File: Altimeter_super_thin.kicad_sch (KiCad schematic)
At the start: 58 parts, among them IC1 XTSD02GLGEAG, J1 Conn_01x04_Male, J2 Conn_01x02_Male, Q1 PMV20ENR, U1 150044M155220, U2 ESP32-S3, U4 DPS310, Y1 40MHz±10ppm

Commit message: initial stage of reitteration
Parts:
- removed C12: 4.2pF, Capacitor_SMD:C_0402_1005Metric, symbol Device:C_Small
- removed R8: 47.5, Resistor_SMD:R_0402_1005Metric, symbol Device:R_Small
- IC1: footprint iclr:SOTFL50P160X60-8N -> iclr:SON127P800X600X95-8N
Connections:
- net +3.3V is gone; now on net +3V3: U1.1 (V)
- no-connect marks 21 -> 22
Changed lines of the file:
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@@
 (kicad_sch (version 20230121) (generator eeschema)
   (paper "A4")
-  (junction (at 39.37 21.59) (diameter 0) (color 0 0 0 0)
-  )
   (junction (at 59.69 142.24) (diameter 0) (color 0 0 0 0)
   )
@@
   )
   (junction (at 69.85 135.89) (diameter 0) (color 0 0 0 0)
+  )
+  (junction (at 40.64 21.59) (diameter 0) (color 0 0 0 0)
   )
   (junction (at 271.78 52.07) (diameter 0) (color 0 0 0 0)
@@
   (no_connect (at 135.89 72.39))
   (no_connect (at 135.89 113.03))
+  (no_connect (at 69.85 62.23))
   (no_connect (at 135.89 82.55))
   (no_connect (at 135.89 85.09))
@@
     (stroke (width 0) (type default))
   )
-  (wire (pts (xy 68.58 62.23) (xy 69.85 62.23))
-    (stroke (width 0) (type default))
-  )
   (wire (pts (xy 27.94 21.59) (xy 30.48 21.59))
     (stroke (width 0) (type default))
@@
     (stroke (width 0) (type default))
   )
-  (wire (pts (xy 50.8 62.23) (xy 54.61 62.23))
-    (stroke (width 0) (type default))
-  )
   (wire (pts (xy 210.82 93.98) (xy 210.82 59.69))
     (stroke (width 0) (type default))
@@
     (stroke (width 0) (type default))
   )
-  (wire (pts (xy 59.69 62.23) (xy 63.5 62.23))
-    (stroke (width 0) (type default))
-  )
   (wire (pts (xy 34.29 167.64) (xy 34.29 165.1))
     (stroke (width 0) (type default))
@@
     (stroke (width 0) (type default))
   )
-  (wire (pts (xy 35.56 21.59) (xy 39.37 21.59))
+  (wire (pts (xy 35.56 21.59) (xy 40.64 21.59))
     (stroke (width 0) (type default))
   )
@@
     (stroke (width 0) (type default))
   )
+  (wire (pts (xy 40.64 21.59) (xy 44.45 21.59))
+    (stroke (width 0) (type default))
+  )
   (wire (pts (xy 201.93 80.01) (xy 233.68 80.01))
     (stroke (width 0) (type default))
@@
   )
   (wire (pts (xy 167.64 127) (xy 167.64 132.08))
-    (stroke (width 0) (type default))
-  )
-  (wire (pts (xy 39.37 21.59) (xy 44.45 21.59))
     (stroke (width 0) (type default))
   )
@@
     )
   )
-  (symbol (lib_id "power:+3.3V") (at 39.37 21.59 0) (unit 1)
-    (in_bom yes) (on_board yes) (dnp no)
-    (property "Reference" "#PWR08" (at 39.37 25.4 0)
-      (effects (font (size 1.27 1.27)) hide)
-    )
-    (property "Value" "+3.3V" (at 39.751 17.1958 0)
-      (effects (font (size 1.27 1.27)))
-    )
-    (property "Footprint" "" (at 39.37 21.59 0)
-      (effects (font (size 1.27 1.27)) hide)
-    )
-    (property "Datasheet" "" (at 39.37 21.59 0)
-      (effects (font (size 1.27 1.27)) hide)
-    )
-    (pin "1")
-    (instances
-      (project "Altimeter"
-        (path "/7db990e4-92e1-4f99-b4d2-435bbec1ba83"
-          (reference "#PWR08") (unit 1)
-        )
-      )
-    )
-  )
   (symbol (lib_id "Device:LED_Small") (at 54.61 21.59 180) (unit 1)
     (in_bom yes) (on_board yes) (dnp no)
@@
     )
   )
+  (symbol (lib_id "power:+3V3") (at 19.05 69.85 0) (unit 1)
+    (in_bom yes) (on_board yes) (dnp no)
+    (property "Reference" "#PWR09" (at 19.05 73.66 0)
+      (effects (font (size 1.27 1.27)) hide)
+    )
+    (property "Value" "+3V3" (at 15.24 68.58 0)
+      (effects (font (size 1.27 1.27)))
+    )
+    (property "Footprint" "" (at 19.05 69.85 0)
+      (effects (font (size 1.27 1.27)) hide)
+    )
+    (property "Datasheet" "" (at 19.05 69.85 0)
+      (effects (font (size 1.27 1.27)) hide)
+    )
+    (pin "1")
+    (instances
+      (project "Altimeter"
+        (path "/7db990e4-92e1-4f99-b4d2-435bbec1ba83"
+          (reference "#PWR09") (unit 1)
+        )
+      )
+    )
+  )
   (symbol (lib_id "Connector:TestPoint") (at 69.85 118.11 90) (unit 1)
     (in_bom yes) (on_board yes) (dnp no)
@@
       (effects (font (size 1.27 1.27)))
     )
-    (property "Footprint" "iclr:SOTFL50P160X60-8N" (at 39.37 96.52 0)
+    (property "Footprint" "iclr:SON127P800X600X95-8N" (at 39.37 96.52 0)
       (effects (font (size 1.27 1.27)) (justify left) hide)
     )
@@
     )
   )
-  (symbol (lib_name "+3.3V_1") (lib_id "power:+3.3V") (at 19.05 69.85 0) (unit 1)
-    (in_bom yes) (on_board yes) (dnp no)
-    (property "Reference" "#PWR09" (at 19.05 73.66 0)
-      (effects (font (size 1.27 1.27)) hide)
-    )
-    (property "Value" "+3.3V" (at 15.24 67.31 0)
-      (effects (font (size 1.27 1.27)))
-    )
-    (property "Footprint" "" (at 19.05 69.85 0)
-      (effects (font (size 1.27 1.27)) hide)
-    )
-    (property "Datasheet" "" (at 19.05 69.85 0)
-      (effects (font (size 1.27 1.27)) hide)
-    )
-    (pin "1")
-    (instances
-      (project "Altimeter"
-        (path "/7db990e4-92e1-4f99-b4d2-435bbec1ba83"
-          (reference "#PWR09") (unit 1)
-        )
-      )
-    )
-  )
   (symbol (lib_id "Device:R") (at 43.18 71.12 90) (unit 1)
     (in_bom yes) (on_board yes) (dnp no)
@@
     )
   )
-  (symbol (lib_id "Device:C_Small") (at 66.04 62.23 90) (unit 1)
-    (in_bom yes) (on_board yes) (dnp no)
-    (property "Reference" "C12" (at 67.31 57.15 90)
-      (effects (font (size 1.27 1.27)) (justify left))
-    )
-    (property "Value" "4.2pF" (at 66.2934 59.2481 90)
-      (effects (font (size 1.27 1.27)) (justify left))
-    )
-    (property "Footprint" "Capacitor_SMD:C_0402_1005Metric" (at 66.04 62.23 0)
-      (effects (font (size 1.27 1.27)) hide)
-    )
-    (property "Datasheet" "~" (at 66.04 62.23 0)
-      (effects (font (size 1.27 1.27)) hide)
-    )
-    (pin "1")
-    (pin "2")
-    (instances
-      (project "Altimeter"
-        (path "/7db990e4-92e1-4f99-b4d2-435bbec1ba83"
-          (reference "C12") (unit 1)
-        )
-      )
-    )
-  )
   (symbol (lib_id "Connector:TestPoint") (at 143.51 80.01 180) (unit 1)
     (in_bom yes) (on_board yes) (dnp no)
@@
         (path "/7db990e4-92e1-4f99-b4d2-435bbec1ba83"
           (reference "TP10") (unit 1)
+        )
+      )
+    )
+  )
+  (symbol (lib_id "power:+3V3") (at 40.64 21.59 0) (unit 1)
+    (in_bom yes) (on_board yes) (dnp no) (fields_autoplaced)
+    (property "Reference" "#PWR012" (at 40.64 25.4 0)
+      (effects (font (size 1.27 1.27)) hide)
+    )
+    (property "Value" "+3V3" (at 40.64 16.51 0)
+      (effects (font (size 1.27 1.27)))
+    )
+    (property "Footprint" "" (at 40.64 21.59 0)
+      (effects (font (size 1.27 1.27)) hide)
+    )
+    (property "Datasheet" "" (at 40.64 21.59 0)
+      (effects (font (size 1.27 1.27)) hide)
+    )
+    (pin "1")
+    (instances
+      (project "Altimeter"
+        (path "/7db990e4-92e1-4f99-b4d2-435bbec1ba83"
+          (reference "#PWR012") (unit 1)
         )
       )
@@
         )
       )
-    )
-  )
-  (symbol (lib_id "power:GND") (at 50.8 62.23 0) (unit 1)
-    (in_bom yes) (on_board yes) (dnp no)
-    (property "Reference" "#PWR012" (at 50.8 68.58 0)
-      (effects (font (size 1.27 1.27)) hide)
-    )
-    (property "Value" "GND" (at 48.26 66.04 0)
-      (effects (font (size 1.27 1.27)) (justify left))
-    )
-    (property "Footprint" "" (at 50.8 62.23 0)
-      (effects (font (size 1.27 1.27)) hide)
-    )
-    (property "Datasheet" "" (at 50.8 62.23 0)
-      (effects (font (size 1.27 1.27)) hide)
-    )
-    (pin "1")
-    (instances
-      (project "Altimeter"
-        (path "/7db990e4-92e1-4f99-b4d2-435bbec1ba83"
-          (reference "#PWR012") (unit 1)
-        )
-      )
-    )
-  )
-  (symbol (lib_id "Device:R_Small") (at 57.15 62.23 90) (unit 1)
-    (in_bom yes) (on_board yes) (dnp no)
-    (property "Reference" "R8" (at 57.15 57.15 90)
-      (effects (font (size 1.27 1.27)))
-    )
-    (property "Value" "47.5" (at 57.15 59.69 90)
-      (effects (font (size 1.27 1.27)))
-    )
-    (property "Footprint" "Resistor_SMD:R_0402_1005Metric" (at 57.15 62.23 0)
-      (effects (font (size 1.27 1.27)) hide)
-    )
-    (property "Datasheet" "~" (at 57.15 62.23 0)
-      (effects (font (size 1.27 1.27)) hide)
-    )
-    (pin "1")
-    (pin "2")
-    (instances
-      (project "Altimeter"
-        (path "/7db990e4-92e1-4f99-b4d2-435bbec1ba83"
-          (reference "R8") (unit 1)
-        )
-      )

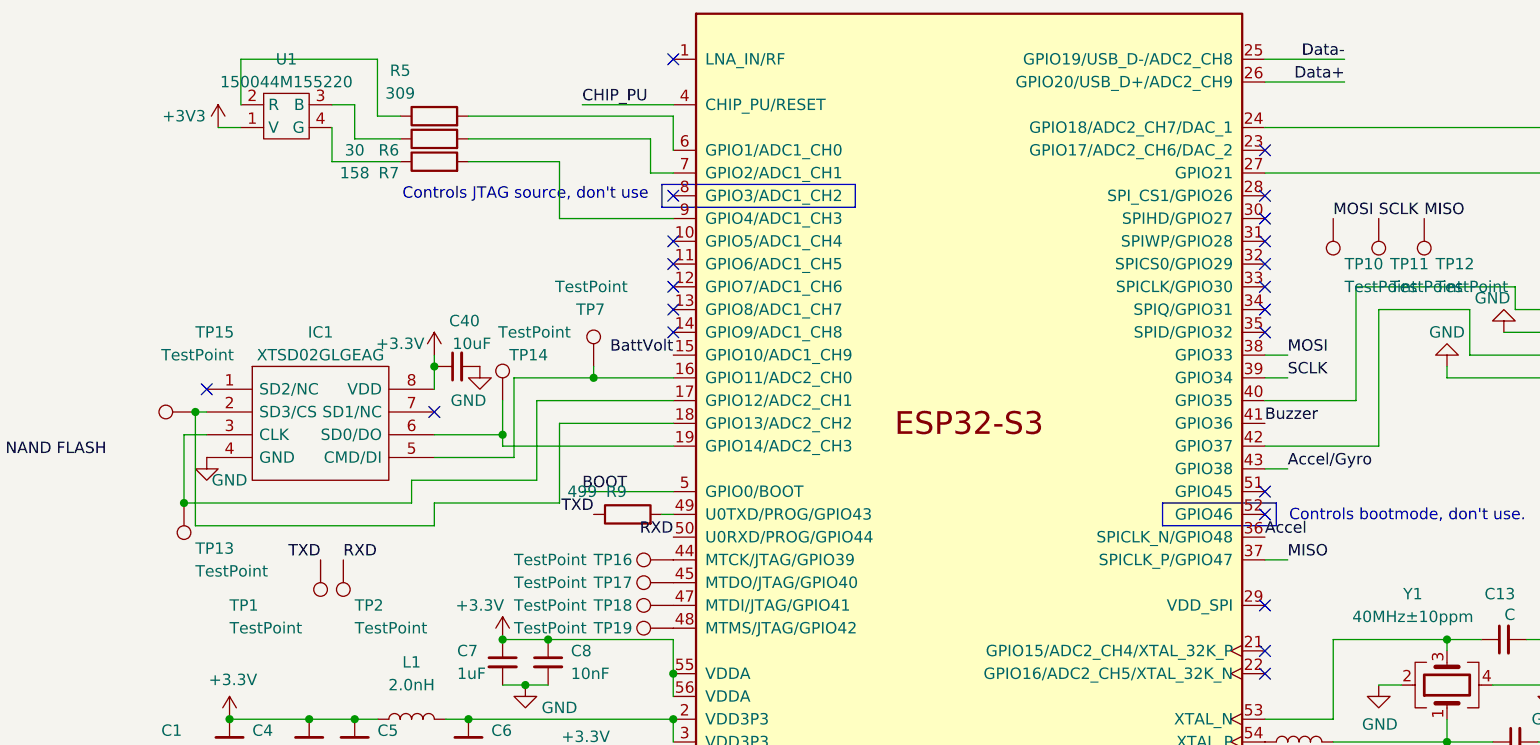
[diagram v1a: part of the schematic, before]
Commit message: rerouted spi bus and changed NAND
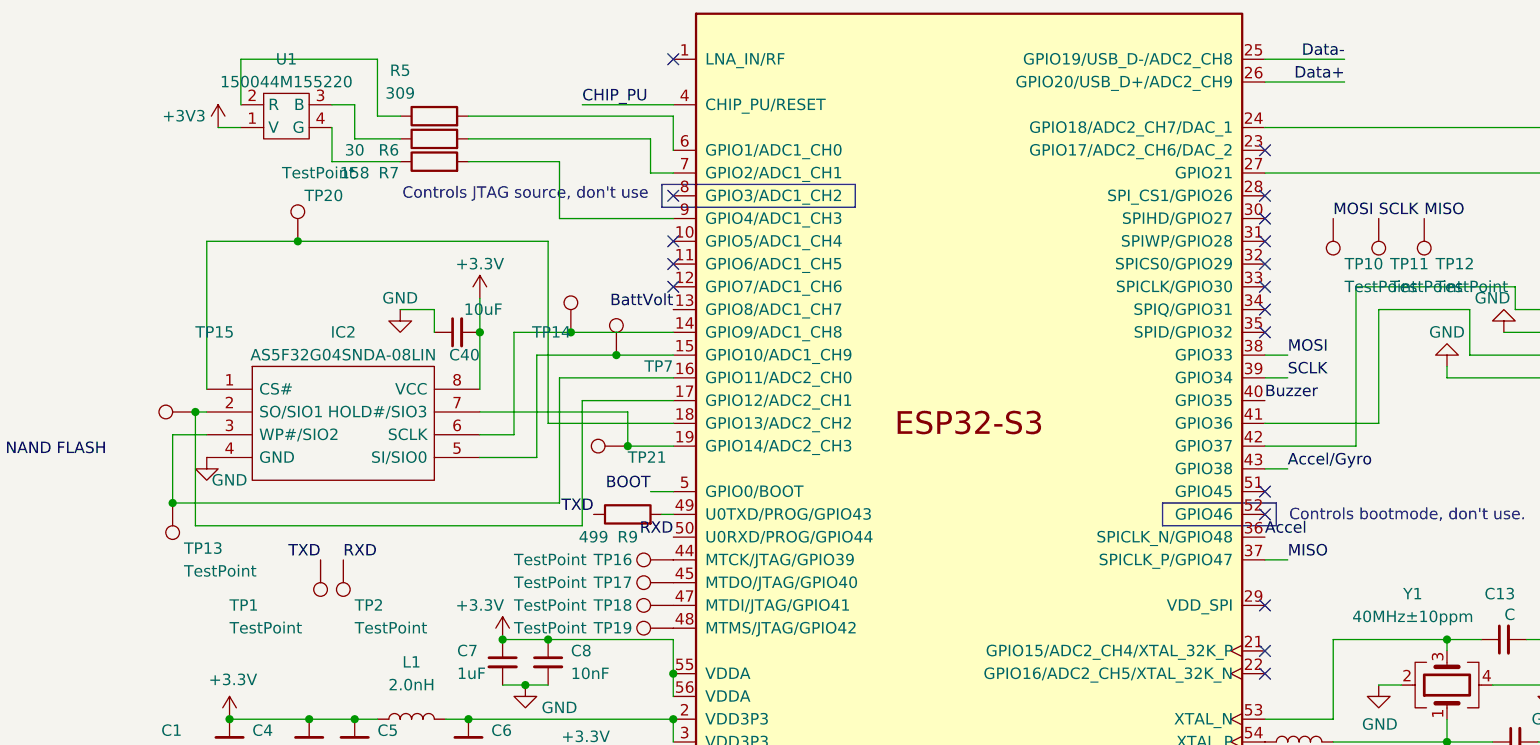
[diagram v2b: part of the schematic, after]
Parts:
- removed IC1: XTSD02GLGEAG, iclr:SON127P800X600X95-8N, symbol chest:XTSD08GLGEAG
- added IC2: AS5F32G04SNDA-08LIN, iclr:SON127P600X800X65-8N, symbol chest:XTSD08GLGEAG
- added TP20, TP21: TestPoint, TestPoint:TestPoint_Pad_D1.0mm, symbol Connector:TestPoint
- H1, H2, H3, H4: footprint MountingHole:MountingHole_3.2mm_M3_DIN965_Pad -> MountingHole:MountingHole_3.2mm_M3_DIN965
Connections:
- net +3V3: now also C40.2, IC2.8 (VCC); no longer C40.1
- net BattVolt: now also U2.13 (GPIO8/ADC1_CH7); no longer U2.15 (GPIO10/ADC1_CH9)
- net Buzzer: now also U2.40 (GPIO35); no longer U2.41 (GPIO36)
- net GND: now also C40.1, IC2.4 (GND); no longer C40.2
- net at TP15.1: now also U2.17 (GPIO12/ADC2_CH1), IC2.2 (SO/SIO1); no longer U2.18 (GPIO13/ADC2_CH2)
- net at TP13.1: now also U2.16 (GPIO11/ADC2_CH0), IC2.3 (WP#/SIO2); no longer U2.17 (GPIO12/ADC2_CH1)
- net at TP7.1: now also U2.15 (GPIO10/ADC1_CH9), IC2.5 (SI/SIO0); no longer U2.16 (GPIO11/ADC2_CH0)
- net at U2.19 (GPIO14/ADC2_CH3): now also IC2.7 (HOLD#/SIO3), TP21.1; no longer TP14.1
- net at J1.2 (Pin_2): now also U2.41 (GPIO36); no longer U2.42 (GPIO37)
- net at J1.4 (Pin_4): now also U2.42 (GPIO37); no longer U2.40 (GPIO35)
- net at U2.14 (GPIO9/ADC1_CH8): now also TP14.1, IC2.6 (SCLK)
- new net: IC2.1 (CS#), TP20.1, U2.18 (GPIO13/ADC2_CH2)
- no-connect marks 22 -> 18
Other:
- moved on the sheet: C40, TP13, TP14, TP7
